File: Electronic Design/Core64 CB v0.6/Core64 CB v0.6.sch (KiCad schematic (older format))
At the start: 20 parts, among them J1 Digi-Key 77311-420-36LF-ND, J2 Digi-Key 77311-420-36LF-ND, U1 SI7210-B-01, U2 SI7210-B-02, U3 SI7210-B-03, U4 SI7210-B-04, U5 BH1730FVC

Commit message: Update P/N for 20 pin headers
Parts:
- J1, J2: value Digi-Key 77311-420-36LF-ND -> 929834-04-36-RK; Alt. Manufacturer (none) -> Amphenol ICC (FCI); Alt. Mfg P/N (none) -> 77311-420-36LF; Manufacturer (none) -> 3M; Mfg P/N (none) -> 929834-04-36-RK
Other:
- note added: "Cut header 36-pin into\ntwo 16-pin headers,\ninstall centered with two\npins on each end not inserted."
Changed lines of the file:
@@
 P 8550 1800
 F 0 "J2" H 8550 2850 50  0000 C CNN
-F 1 "Digi-Key 77311-420-36LF-ND" H 9400 2850 50  0000 C CNN
+F 1 "929834-04-36-RK" H 9400 2850 50  0000 C CNN
 F 2 "Connector_PinHeader_2.54mm:PinHeader_1x20_P2.54mm_Vertical_SMD_and_TH_Pin1Right" H 8550 1800 50  0001 C CNN
 F 3 "~" H 8550 1800 50  0001 C CNN
+F 4 "Amphenol ICC (FCI)" H 8550 1800 50  0001 C CNN "Alt. Manufacturer"
+F 5 "77311-420-36LF" H 8550 1800 50  0001 C CNN "Alt. Mfg P/N"
+F 6 "3M" H 8550 1800 50  0001 C CNN "Manufacturer"
+F 7 "929834-04-36-RK" H 8550 1800 50  0001 C CNN "Mfg P/N"
 	1    8550 1800
 	-1   0    0    -1
@@
 P 2700 1850
 F 0 "J1" H 2700 2950 50  0000 C CNN
-F 1 "Digi-Key 77311-420-36LF-ND" H 3550 2950 50  0000 C CNN
+F 1 "929834-04-36-RK" H 3550 2950 50  0000 C CNN
 F 2 "Connector_PinHeader_2.54mm:PinHeader_1x20_P2.54mm_Vertical_SMD_and_TH_Pin1Right" H 2700 1850 50  0001 C CNN
 F 3 "~" H 2700 1850 50  0001 C CNN
+F 4 "Amphenol ICC (FCI)" H 2700 1850 50  0001 C CNN "Alt. Manufacturer"
+F 5 "77311-420-36LF" H 2700 1850 50  0001 C CNN "Alt. Mfg P/N"
+F 6 "3M" H 2700 1850 50  0001 C CNN "Manufacturer"
+F 7 "929834-04-36-RK" H 2700 1850 50  0001 C CNN "Mfg P/N"
 	1    2700 1850
 	1    0    0    -1
@@
 Text Notes 7300 5600 0    50   ~ 0
 BOTTOM MOUNTED
+Text Notes 650  1250 0    50   ~ 0
+Cut header 36-pin into\ntwo 16-pin headers,\ninstall centered with two\npins on each end not inserted.
 $EndSCHEMATC

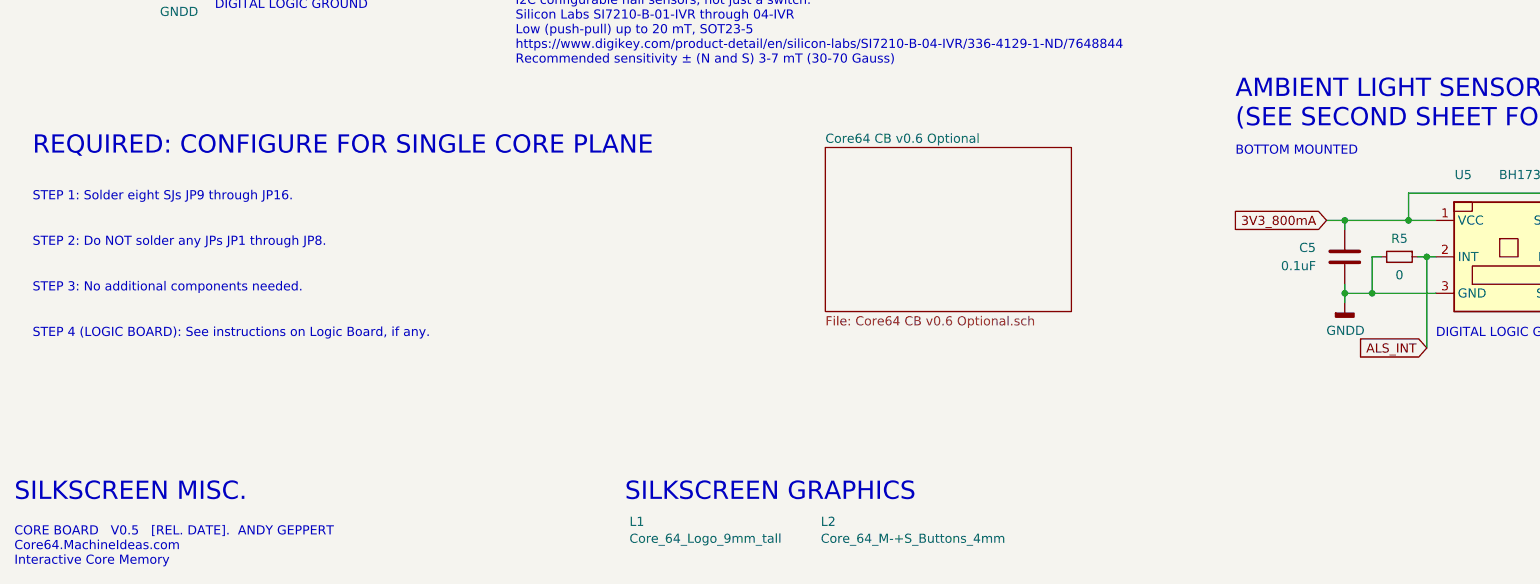
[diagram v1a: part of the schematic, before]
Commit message: CB refine silkscreen, change center ALS BH1730 opening to drill hole and remove center solder pad, clean-up ref. des. numbers
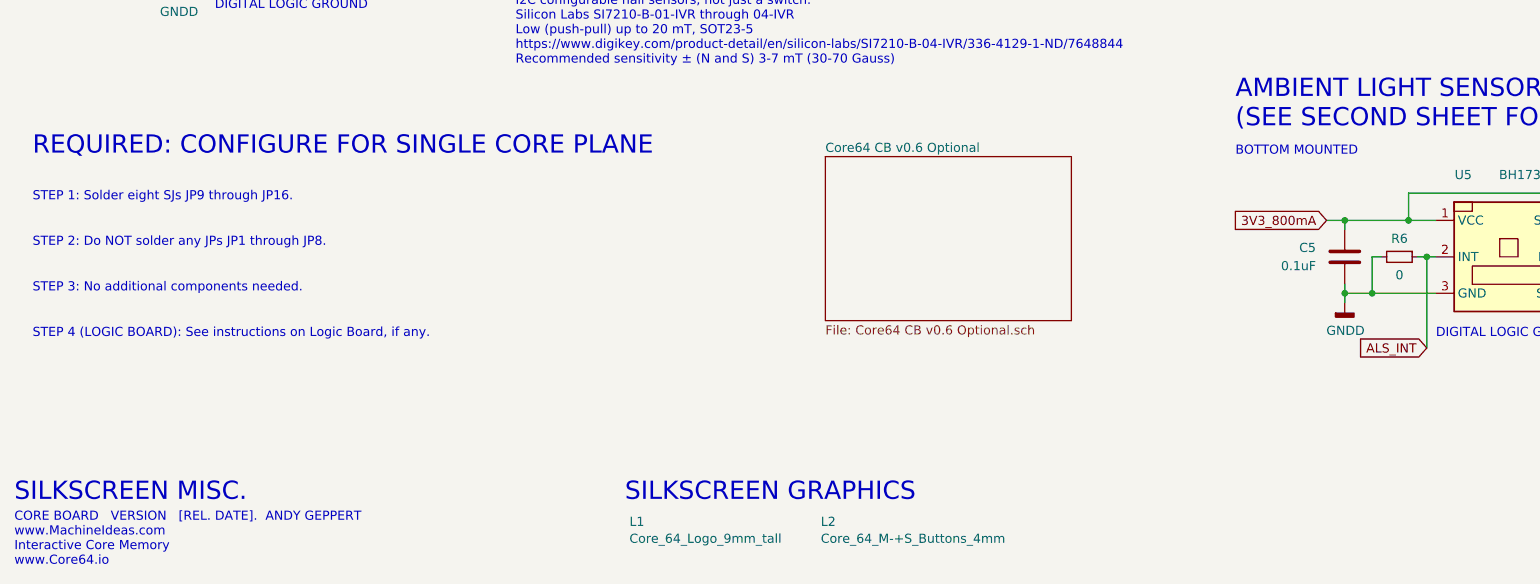
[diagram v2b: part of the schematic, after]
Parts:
- renumbered R5 to R6
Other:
- note added: "CORE BOARD VERSION [REL. DATE]. ANDY GEPPERT \nwww.MachineIdeas.com\nInteractive Core Memory\nwww.Core64.io"
- note removed: "CORE BOARD V0.5 [REL. DATE]. ANDY GEPPERT \nCore64.MachineIdeas.com\nInteractive Core Memory"
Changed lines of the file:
@@
 Sheet 1 2
 Title "Core64 CB (Core Board)"
-Date "2021-06-07"
+Date "2021-08-08"
 Rev "0.6"
 Comp "Concept and design by Andy Geppert @ www.MachineIdeas.com"
@@
 SILKSCREEN:\nPixel 56-63->
 Text Notes 600  7850 0    50   ~ 0
-CORE BOARD   V0.5   [REL. DATE].  ANDY GEPPERT   \nCore64.MachineIdeas.com\nInteractive Core Memory
+CORE BOARD   VERSION   [REL. DATE].  ANDY GEPPERT   \nwww.MachineIdeas.com\nInteractive Core Memory\nwww.Core64.io
 Text GLabel 3300 2350 2    50   Output ~ 0
 PLANE_8
@@
 Connection ~ 7900 6350
 $Comp
-L Device:R_Small R5
+L Device:R_Small R6
 U 1 1 602E2405
 P 8200 6150
-F 0 "R5" V 8100 6150 50  0000 C CNN
+F 0 "R6" V 8100 6150 50  0000 C CNN
 F 1 "0" V 8300 6150 50  0000 C CNN
 F 2 "Resistor_SMD:R_0805_2012Metric" H 8200 6150 50  0001 C CNN
@@
 	8350 6150 8300 6150
 $Sheet
-S 5050 5550 1350 900
+S 5050 5600 1350 900
 U 604D6360
 F0 "Core64 CB v0.6 Optional" 50

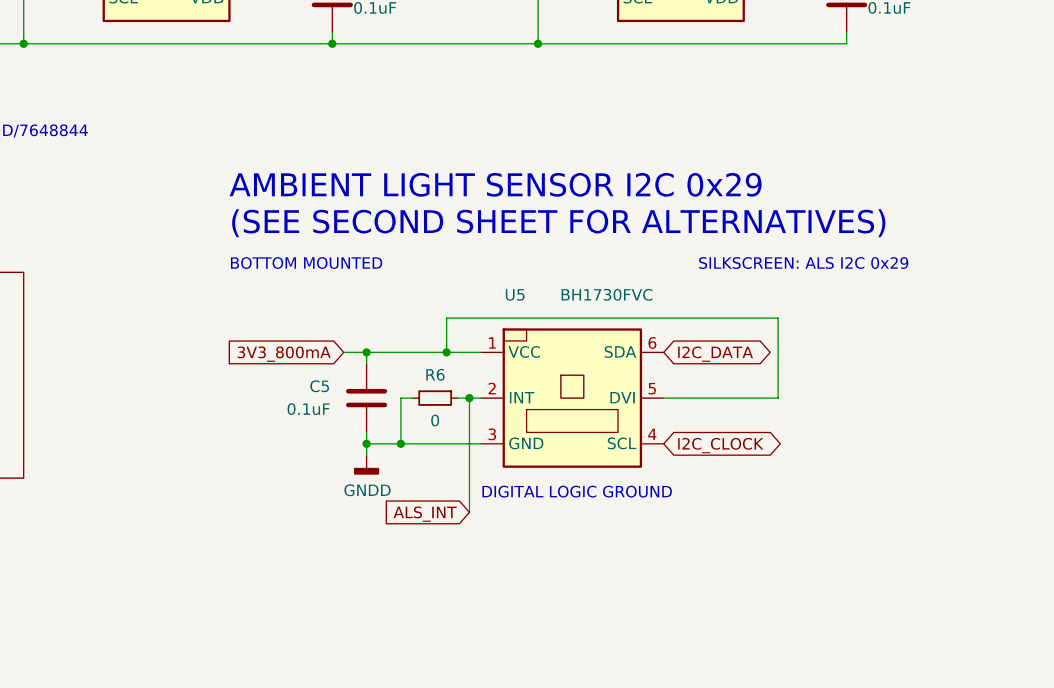
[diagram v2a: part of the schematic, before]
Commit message: Core Board V0.6 remove bottom ALS, add new top ALS+PROX option
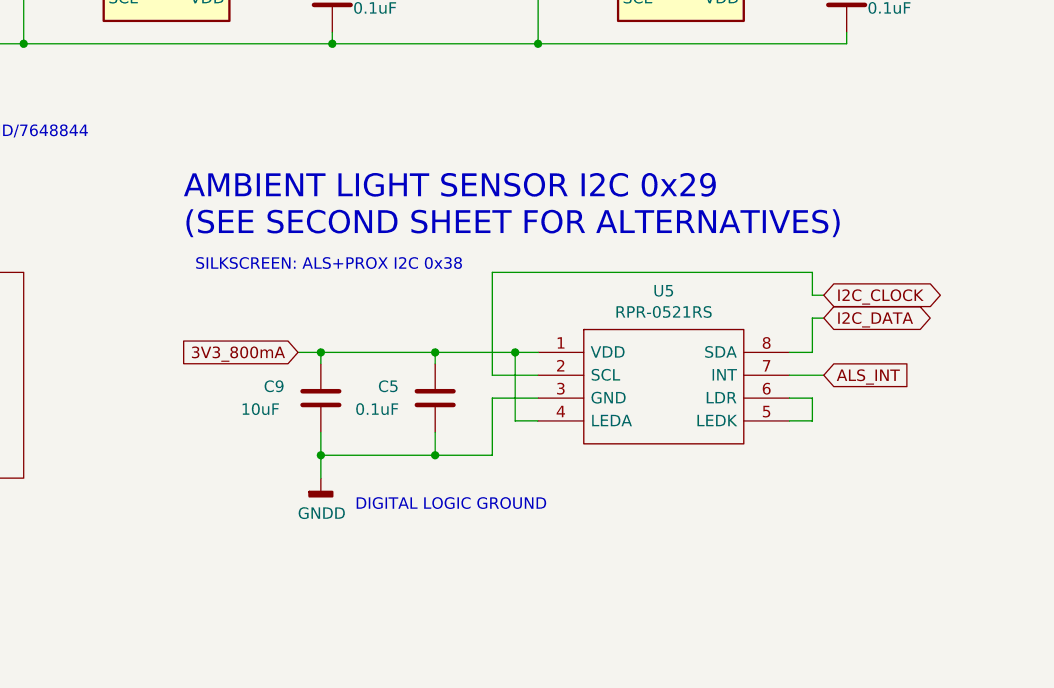
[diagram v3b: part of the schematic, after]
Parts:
- removed R6: 0, Resistor_SMD:R_0805_2012Metric, symbol Device:R_Small
- removed U5: BH1730FVC, ALS_BH1730:BH1730-backside, symbol Core_64_KiCad_Library:BH1730FVC
- added C9: 10uF, Capacitor_SMD:C_0805_2012Metric, symbol Device:C
- added U5: RPR-0521RS, Rohm_RPR-0521RS:RPR0521RS, symbol RPR-0521RS:RPR-0521RS
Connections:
- net 3V3_800mA: now also C9.1, U5.1 (VDD), U5.4 (LEDA)
- net ALS_INT: now also U5.7 (INT)
- net GNDD: now also C9.2, U5.3 (GND)
- net I2C_CLOCK: now also U5.2 (SCL)
- net I2C_DATA: now also U5.8 (SDA)
- new net: U5.5 (LEDK), U5.6 (LDR)
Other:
- note added: "SILKSCREEN: ALS+PROX I2C 0x38"
- note removed: "BOTTOM MOUNTED"
- note removed: "SILKSCREEN: ALS I2C 0x29"
- moved on the sheet: C5
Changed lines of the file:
@@
 Wire Wire Line
 	8350 3000 8050 3000
-Text Notes 9350 5600 0    50   ~ 0
-SILKSCREEN: ALS I2C 0x29
+Text Notes 7150 5600 0    50   ~ 0
+SILKSCREEN: ALS+PROX I2C 0x38
 $Comp
 L power:GNDD #PWR05
@@
 Wire Wire Line
 	7750 2600 8350 2600
-Text Notes 7300 5450 0    100  ~ 0
+Text Notes 7100 5450 0    100  ~ 0
 AMBIENT LIGHT SENSOR I2C 0x29\n(SEE SECOND SHEET FOR ALTERNATIVES)
 Text Notes 3950 7500 0    100  ~ 0
@@
 NoConn ~ 2900 2850
 $Comp
-L Core_64_KiCad_Library:BH1730FVC U5
-U 1 1 604130EC
-P 8800 6150
-F 0 "U5" H 8550 6600 50  0000 C CNN
-F 1 "BH1730FVC" H 8950 6600 50  0000 C CNN
-F 2 "ALS_BH1730:BH1730-backside" H 8800 6600 50  0001 C CNN
-F 3 "http://optoelectronics.liteon.com/upload/download/DS86-2013-0004/LTR-303ALS-01_DS_V1.pdf" H 8500 6500 50  0001 C CNN
-F 4 "C79616" H 8800 6150 50  0001 C CNN "LCSC"
-	1    8800 6150
-	1    0    0    -1
-$EndComp
-$Comp
 L Device:C C5
 U 1 1 60495262
-P 7900 6150
-F 0 "C5" H 7650 6200 50  0000 L CNN
-F 1 "0.1uF" H 7550 6100 50  0000 L CNN
-F 2 "Capacitor_SMD:C_0805_2012Metric" H 7938 6000 50  0001 C CNN
-F 3 "~" H 7900 6150 50  0001 C CNN
-F 4 "C396718" H 7900 6150 50  0001 C CNN "LCSC"
-	1    7900 6150
-	1    0    0    -1
-$EndComp
-Text Notes 8400 6600 0    50   ~ 0
+P 8200 6150
+F 0 "C5" H 7950 6200 50  0000 L CNN
+F 1 "0.1uF" H 7850 6100 50  0000 L CNN
+F 2 "Capacitor_SMD:C_0805_2012Metric" H 8238 6000 50  0001 C CNN
+F 3 "~" H 8200 6150 50  0001 C CNN
+F 4 "C396718" H 8200 6150 50  0001 C CNN "LCSC"
+	1    8200 6150
+	1    0    0    -1
+$EndComp
+Text Notes 7850 6650 0    50   ~ 0
 DIGITAL LOGIC GROUND
 $Comp
 L power:GNDD #PWR01
 U 1 1 60495269
-P 7900 6400
-F 0 "#PWR01" H 7900 6150 50  0001 C CNN
-F 1 "GNDD" H 7904 6245 50  0000 C CNN
-F 2 "" H 7900 6400 50  0001 C CNN
-F 3 "" H 7900 6400 50  0001 C CNN
-	1    7900 6400
-	1    0    0    -1
-$EndComp
-Wire Wire Line
-	7900 6350 8050 6350
-Wire Wire Line
-	7900 6350 7900 6400
-Wire Wire Line
-	7900 5950 7900 6000
-Text GLabel 7800 5950 0    50   Input ~ 0
+P 7700 6500
+F 0 "#PWR01" H 7700 6250 50  0001 C CNN
+F 1 "GNDD" H 7704 6345 50  0000 C CNN
+F 2 "" H 7700 6500 50  0001 C CNN
+F 3 "" H 7700 6500 50  0001 C CNN
+	1    7700 6500
+	1    0    0    -1
+$EndComp
+Wire Wire Line
+	8200 5950 8200 6000
+Text GLabel 7600 5950 0    50   Input ~ 0
 3V3_800mA
-Text GLabel 9200 5950 2    50   BiDi ~ 0
-I2C_DATA
-Text GLabel 9200 6350 2    50   BiDi ~ 0
+Text GLabel 9900 5700 2    50   BiDi ~ 0
 I2C_CLOCK
 Wire Wire Line
-	7900 5950 7800 5950
-Connection ~ 7900 5950
-Wire Wire Line
-	7900 6350 7900 6300
-Connection ~ 7900 6350
-$Comp
-L Device:R_Small R6
-U 1 1 602E2405
-P 8200 6150
-F 0 "R6" V 8100 6150 50  0000 C CNN
-F 1 "0" V 8300 6150 50  0000 C CNN
-F 2 "Resistor_SMD:R_0805_2012Metric" H 8200 6150 50  0001 C CNN
-F 3 "~" H 8200 6150 50  0001 C CNN
-F 4 "C115306" V 8200 6150 50  0001 C CNN "LCSC"
-	1    8200 6150
-	0    1    1    0
-$EndComp
-Wire Wire Line
-	8400 6150 8350 6150
-Wire Wire Line
-	8100 6150 8050 6150
-Wire Wire Line
-	8250 5950 8250 5800
-Wire Wire Line
-	8250 5800 9700 5800
-Wire Wire Line
-	9700 5800 9700 6150
-Connection ~ 8250 5950
-Wire Wire Line
-	8250 5950 8400 5950
-Wire Wire Line
-	9200 6150 9700 6150
-Wire Wire Line
-	7900 5950 8250 5950
-Wire Wire Line
-	8050 6150 8050 6350
-Connection ~ 8050 6350
-Wire Wire Line
-	8050 6350 8400 6350
-Wire Wire Line
-	8350 6150 8350 6650
-Connection ~ 8350 6150
-Wire Wire Line
-	8350 6150 8300 6150
+	8200 5950 7700 5950
+Connection ~ 8200 5950
+Wire Wire Line
+	8200 6400 8200 6300
 $Sheet
 S 5050 5600 1350 900
@@
 F1 "Core64 CB v0.6 Optional.sch" 50
 $EndSheet
-Text GLabel 8350 6650 0    50   Input ~ 0
+Text GLabel 9900 6050 2    50   Input ~ 0
 ALS_INT
 Wire Notes Line
@@
 Wire Notes Line
 	2150 1100 2150 2250
-Text Notes 7300 5600 0    50   ~ 0
-BOTTOM MOUNTED
 Text Notes 650  1250 0    50   ~ 0
 Cut header 36-pin into\ntwo 16-pin headers,\ninstall centered with two\npins on each end not inserted.
+Wire Wire Line
+	8650 6050 8450 6050
+Wire Wire Line
+	8200 5950 8550 5950
+Wire Wire Line
+	9900 5700 9850 5700
+Wire Wire Line
+	9850 5700 9850 5600
+Wire Wire Line
+	8450 5600 8450 6050
+Wire Wire Line
+	8650 6150 8450 6150
+Wire Wire Line
+	8450 6150 8450 6400
+Wire Wire Line
+	8450 5600 9850 5600
+Wire Wire Line
+	9750 6250 9850 6250
+Wire Wire Line
+	9850 6150 9750 6150
+Wire Wire Line
+	8650 6250 8550 6250
+Wire Wire Line
+	8550 6250 8550 5950
+Connection ~ 8550 5950
+Wire Wire Line
+	8550 5950 8650 5950
+Wire Wire Line
+	8200 6400 8450 6400
+$Comp
+L Device:C C9
+U 1 1 6164A6E2
+P 7700 6150
+F 0 "C9" H 7450 6200 50  0000 L CNN
+F 1 "10uF" H 7350 6100 50  0000 L CNN
+F 2 "Capacitor_SMD:C_0805_2012Metric" H 7738 6000 50  0001 C CNN
+F 3 "~" H 7700 6150 50  0001 C CNN
+F 4 "C396718" H 7700 6150 50  0001 C CNN "LCSC"
+	1    7700 6150
+	1    0    0    -1
+$EndComp
+Wire Wire Line
+	7700 6000 7700 5950
+Wire Wire Line
+	7600 5950 7700 5950
+Connection ~ 7700 5950
+Wire Wire Line
+	9850 6250 9850 6150
+$Comp
+L RPR-0521RS:RPR-0521RS U5
+U 1 1 61599E59
+P 8650 5950
+F 0 "U5" H 9200 6218 50  0000 C CNN
+F 1 "RPR-0521RS" H 9200 6125 50  0000 C CNN
+F 2 "Rohm_RPR-0521RS:RPR0521RS" H 9600 6050 50  0001 L CNN
+F 3 "http://rohmfs.rohm.com/en/products/databook/datasheet/opto/optical_sensor/opto_module/rpr-0521rs-e.pdf" H 9600 5950 50  0001 L CNN
+F 4 " ALS w/prx 1.8V logic w/ IrLED driver" H 9600 5850 50  0001 L CNN "Description"
+F 5 "1.35" H 9600 5750 50  0001 L CNN "Height"
+F 6 "ROHM Semiconductor" H 9600 5650 50  0001 L CNN "Manufacturer_Name"
+F 7 "RPR-0521RS" H 9600 5550 50  0001 L CNN "Manufacturer_Part_Number"
+F 8 "755-RPR-0521RS" H 9600 5450 50  0001 L CNN "Mouser Part Number"
+F 9 "https://www.mouser.co.uk/ProductDetail/ROHM-Semiconductor/RPR-0521RS/?qs=pn%2Fzyis3XjF8Rw%252BiP8XjBQ%3D%3D" H 9600 5350 50  0001 L CNN "Mouser Price/Stock"
+F 10 "" H 9600 5250 50  0001 L CNN "Arrow Part Number"
+F 11 "" H 9600 5150 50  0001 L CNN "Arrow Price/Stock"
+	1    8650 5950
+	1    0    0    -1
+$EndComp
+Text GLabel 9900 5800 2    50   BiDi ~ 0
+I2C_DATA
+Wire Wire Line
+	9750 5950 9850 5950
+Wire Wire Line
+	9850 5950 9850 5800
+Wire Wire Line
+	9850 5800 9900 5800
+Wire Wire Line
+	9750 6050 9900 6050
+Wire Wire Line
+	8200 6400 7700 6400
+Wire Wire Line
+	7700 6400 7700 6300
+Connection ~ 8200 6400
+Wire Wire Line
+	7700 6500 7700 6400
+Connection ~ 7700 6400
 $EndSCHEMATC
